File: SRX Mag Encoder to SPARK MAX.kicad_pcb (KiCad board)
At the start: 2 copper layers, 31 x 15.2 mm, 3 parts, among them J1 Conn_01x10_Pin

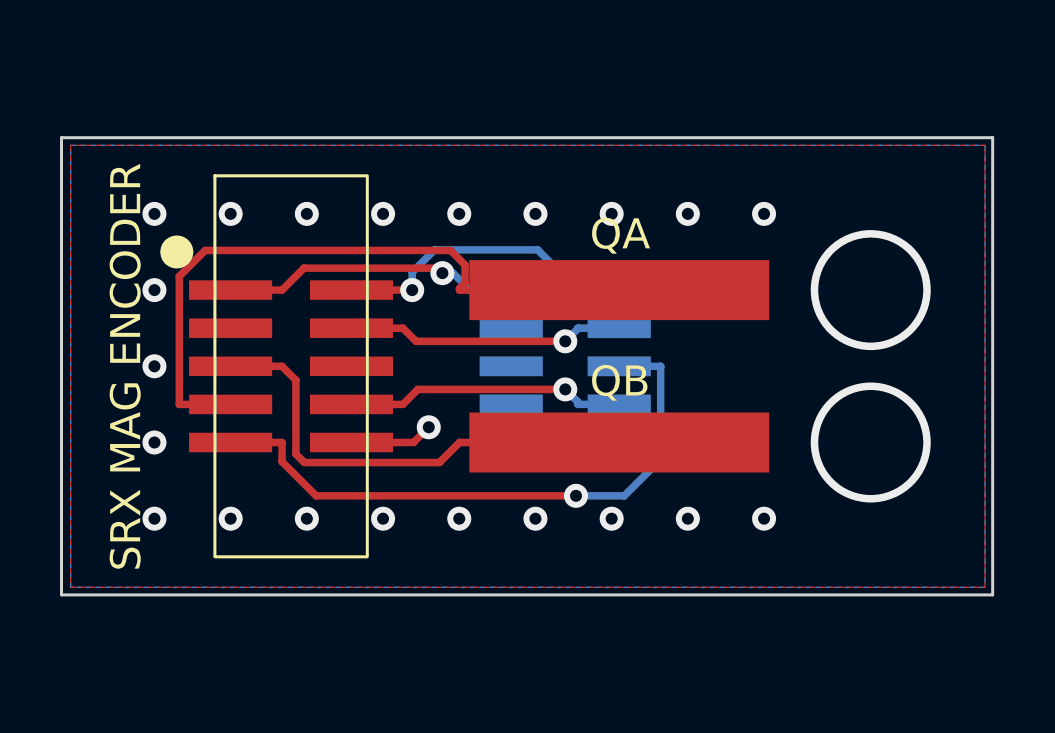
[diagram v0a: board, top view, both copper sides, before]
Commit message: Routed power outputs to solder pads for roborio connection
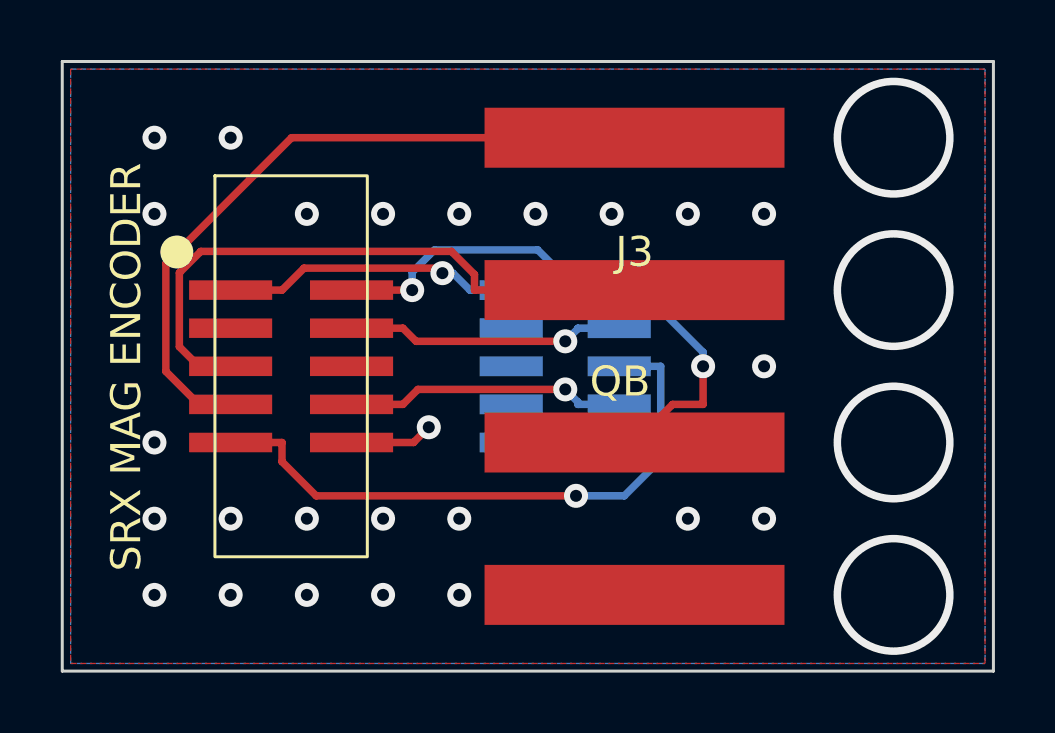
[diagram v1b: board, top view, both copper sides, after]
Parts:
- removed QA: Conn_01x02_Pin, footprints:2 Solder Pads
- added J3: Conn_01x04_Pin, footprints:4 Solder Pads, F.Cu at (176.0, 101.6)
- gave numbers to parts that had none: 1
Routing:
- net +5V: track 10.4 -> 18.6 mm, vias 1 -> 2
- net QB: track 16.0 -> 20.8 mm
- net QA: track 22.3 -> 23.6 mm
- net GND: vias 22 -> 25
- net (no net): vias 2 -> 4
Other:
- board size 31 x 15.2 mm -> 31 x 20.3 mm
